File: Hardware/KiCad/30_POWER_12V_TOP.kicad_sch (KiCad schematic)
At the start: 0 parts

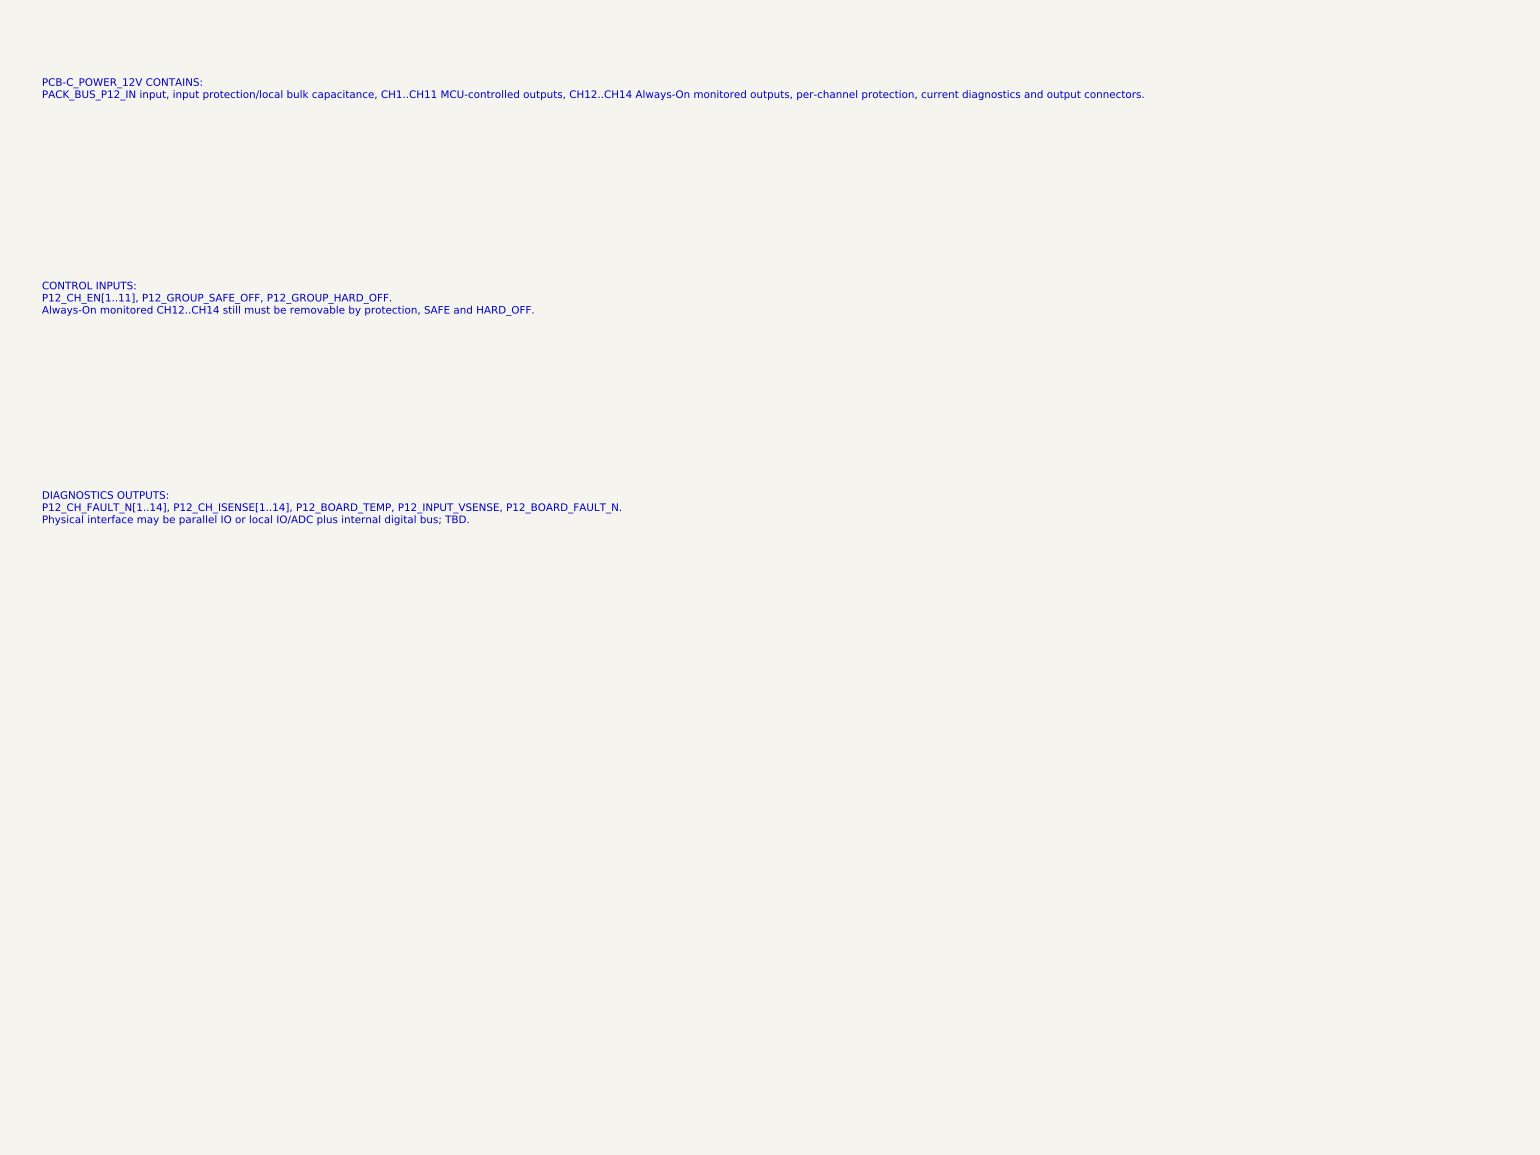
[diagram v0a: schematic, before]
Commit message: hardware: detail all PCB top sheets level A
Convert remaining PCB top sheets to Architecture Level A functional sheets.

Includes PCB-A/BFE_POWER, PCB-B/CTRL_RESERVE, PCB-C/POWER_12V, PCB-D/POWER_5V, PCB-E/LIGHT_POWER, and manifest update.

No component selection, footprints, connector family selection, final pin-count, or PCB layout changes.
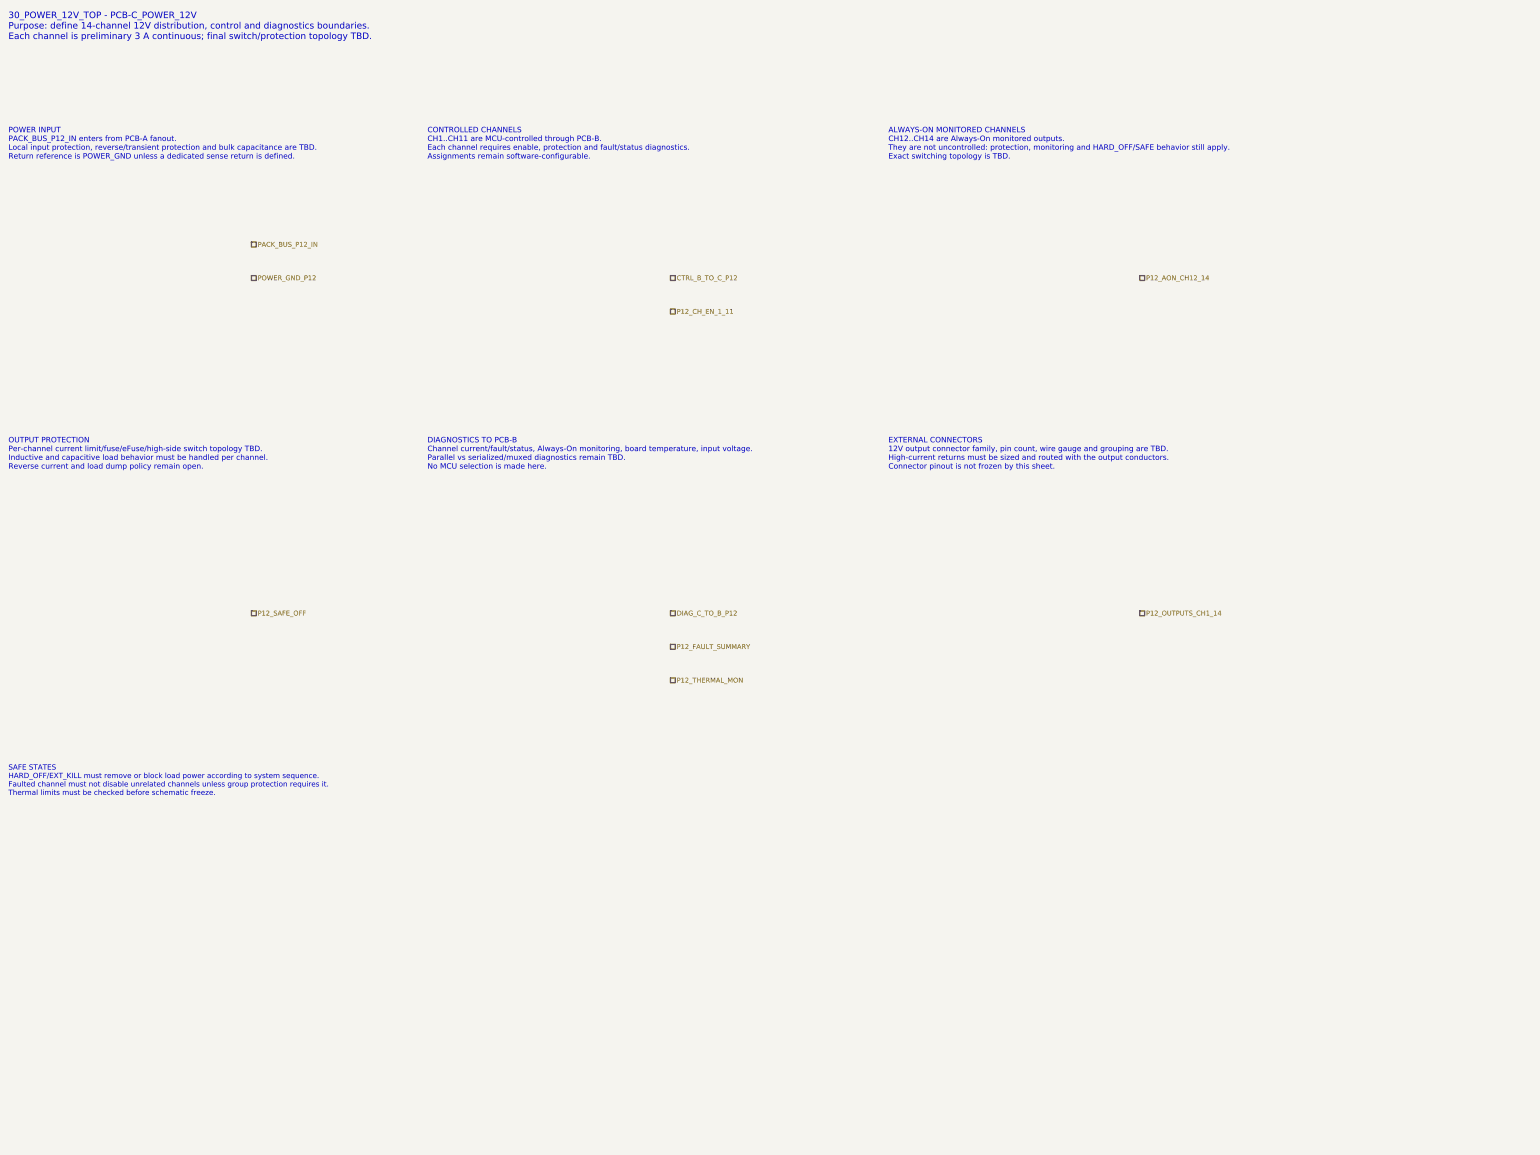
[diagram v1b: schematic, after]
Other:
- note added: "30_POWER_12V_TOP - PCB-C_POWER_12V Purpose: define 14-channel 12V distribution, control and diagnostics boundaries. Each channel is preliminary 3 A continuous; final switch/protection topology TBD."
- note added: "ALWAYS-ON MONITORED CHANNELS CH12..CH14 are Always-On monitored outputs. They are not uncontrolled: protection, monitoring and HARD_OFF/SAFE behavior still apply. Exact switching topology is TBD."
- note added: "CONTROLLED CHANNELS CH1..CH11 are MCU-controlled through PCB-B. Each channel requires enable, protection and fault/status diagnostics. Assignments remain software-configurable."
- note added: "DIAGNOSTICS TO PCB-B Channel current/fault/status, Always-On monitoring, board temperature, input voltage. Parallel vs serialized/muxed diagnostics remain TBD. No MCU selection is made here."
- note added: "EXTERNAL CONNECTORS 12V output connector family, pin count, wire gauge and grouping are TBD. High-current returns must be sized and routed with the output conductors. Connector pinout is not frozen by this sheet."
- note added: "OUTPUT PROTECTION Per-channel current limit/fuse/eFuse/high-side switch topology TBD. Inductive and capacitive load behavior must be handled per channel. Reverse current and load dump policy remain open."
- note added: "POWER INPUT PACK_BUS_P12_IN enters from PCB-A fanout. Local input protection, reverse/transient protection and bulk capacitance are TBD. Return reference is POWER_GND unless a dedicated sense return is defined."
- note added: "SAFE STATES HARD_OFF/EXT_KILL must remove or block load power according to system sequence. Faulted channel must not disable unrelated channels unless group protection requires it. Thermal limits must be checked before schematic freeze."
- note removed: "CONTROL INPUTS: P12_CH_EN[1..11], P12_GROUP_SAFE_OFF, P12_GROUP_HARD_OFF. Always-On monitored CH12..CH14 still must be removable by protection, SAFE and HARD_OFF."
- note removed: "DIAGNOSTICS OUTPUTS: P12_CH_FAULT_N[1..14], P12_CH_ISENSE[1..14], P12_BOARD_TEMP, P12_INPUT_VSENSE, P12_BOARD_FAULT_N. Physical interface may be parallel IO or local IO/ADC plus internal digital bus; TBD."
- note removed: "PCB-C_POWER_12V CONTAINS: PACK_BUS_P12_IN input, input protection/local bulk capacitance, CH1..CH11 MCU-controlled outputs, CH12..CH14 Always-On monitored outputs, per-channel protection, current diagnostics and output connectors."
- company: (none) -> Gonoboben/plataVM
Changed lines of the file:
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@@
 	(title_block
 		(title "30_POWER_12V_TOP - PCB-C_POWER_12V")
-		(date "2026-07-14")
-		(rev "A0")
-		(comment 1 "14-channel 12V distribution, control and diagnostics")
+		(date "2026-07-15")
+		(rev "A1")
+		(company "Gonoboben/plataVM")
+		(comment 1 "Architecture Level A: 14-channel 12V distribution")
+		(comment 2 "No eFuse/high-side switch part numbers or footprints selected")
 	)
-	(text "CONTROL INPUTS:\nP12_CH_EN[1..11], P12_GROUP_SAFE_OFF, P12_GROUP_HARD_OFF.\nAlways-On monitored CH12..CH14 still must be removable by protection, SAFE and HARD_OFF."
+	(text "30_POWER_12V_TOP - PCB-C_POWER_12V\nPurpose: define 14-channel 12V distribution, control and diagnostics boundaries.\nEach channel is preliminary 3 A continuous; final switch/protection topology TBD."
 		(exclude_from_sim no)
-		(at 20 75 0)
-		(effects
-			(font
-				(size 1.8 1.8)
-			)
-			(justify left)
-		)
+		(at 12 10 0)
+		(effects (font (size 1.55 1.55)) (justify left))
+		(uuid "p12-text-0001")
 	)
-	(text "DIAGNOSTICS OUTPUTS:\nP12_CH_FAULT_N[1..14], P12_CH_ISENSE[1..14], P12_BOARD_TEMP, P12_INPUT_VSENSE, P12_BOARD_FAULT_N.\nPhysical interface may be parallel IO or local IO/ADC plus internal digital bus; TBD."
+	(text "POWER INPUT\nPACK_BUS_P12_IN enters from PCB-A fanout.\nLocal input protection, reverse/transient protection and bulk capacitance are TBD.\nReturn reference is POWER_GND unless a dedicated sense return is defined."
 		(exclude_from_sim no)
-		(at 20 125 0)
-		(effects
-			(font
-				(size 1.8 1.8)
-			)
-			(justify left)
-		)
+		(at 12 38 0)
+		(effects (font (size 1.3 1.3)) (justify left))
+		(uuid "p12-text-0002")
 	)
-	(text "PCB-C_POWER_12V CONTAINS:\nPACK_BUS_P12_IN input, input protection/local bulk capacitance, CH1..CH11 MCU-controlled outputs, CH12..CH14 Always-On monitored outputs, per-channel protection, current diagnostics and output connectors."
+	(text "CONTROLLED CHANNELS\nCH1..CH11 are MCU-controlled through PCB-B.\nEach channel requires enable, protection and fault/status diagnostics.\nAssignments remain software-configurable."
 		(exclude_from_sim no)
-		(at 20 25 0)
-		(effects
-			(font
-				(size 1.8 1.8)
-			)
-			(justify left)
-		)
+		(at 112 38 0)
+		(effects (font (size 1.3 1.3)) (justify left))
+		(uuid "p12-text-0003")
 	)
+	(text "ALWAYS-ON MONITORED CHANNELS\nCH12..CH14 are Always-On monitored outputs.\nThey are not uncontrolled: protection, monitoring and HARD_OFF/SAFE behavior still apply.\nExact switching topology is TBD."
+		(exclude_from_sim no)
+		(at 222 38 0)
+		(effects (font (size 1.3 1.3)) (justify left))
+		(uuid "p12-text-0004")
+	)
+	(text "OUTPUT PROTECTION\nPer-channel current limit/fuse/eFuse/high-side switch topology TBD.\nInductive and capacitive load behavior must be handled per channel.\nReverse current and load dump policy remain open."
+		(exclude_from_sim no)
+		(at 12 112 0)
+		(effects (font (size 1.3 1.3)) (justify left))
+		(uuid "p12-text-0005")
+	)
+	(text "DIAGNOSTICS TO PCB-B\nChannel current/fault/status, Always-On monitoring, board temperature, input voltage.\nParallel vs serialized/muxed diagnostics remain TBD.\nNo MCU selection is made here."
+		(exclude_from_sim no)
+		(at 112 112 0)
+		(effects (font (size 1.3 1.3)) (justify left))
+		(uuid "p12-text-0006")
+	)
+	(text "EXTERNAL CONNECTORS\n12V output connector family, pin count, wire gauge and grouping are TBD.\nHigh-current returns must be sized and routed with the output conductors.\nConnector pinout is not frozen by this sheet."
+		(exclude_from_sim no)
+		(at 222 112 0)
+		(effects (font (size 1.3 1.3)) (justify left))
+		(uuid "p12-text-0007")
+	)
+	(text "SAFE STATES\nHARD_OFF/EXT_KILL must remove or block load power according to system sequence.\nFaulted channel must not disable unrelated channels unless group protection requires it.\nThermal limits must be checked before schematic freeze."
+		(exclude_from_sim no)
+		(at 12 190 0)
+		(effects (font (size 1.25 1.25)) (justify left))
+		(uuid "p12-text-0008")
+	)
+	(hierarchical_label "PACK_BUS_P12_IN" (shape passive) (exclude_from_sim no) (at 70 62 0) (effects (font (size 1.15 1.15)) (justify left)) (uuid "p12-label-0001"))
+	(hierarchical_label "POWER_GND_P12" (shape passive) (exclude_from_sim no) (at 70 70 0) (effects (font (size 1.15 1.15)) (justify left)) (uuid "p12-label-0002"))
+	(hierarchical_label "CTRL_B_TO_C_P12" (shape passive) (exclude_from_sim no) (at 170 70 0) (effects (font (size 1.15 1.15)) (justify left)) (uuid "p12-label-0003"))
+	(hierarchical_label "P12_CH_EN_1_11" (shape passive) (exclude_from_sim no) (at 170 78 0) (effects (font (size 1.15 1.15)) (justify left)) (uuid "p12-label-0004"))
+	(hierarchical_label "P12_AON_CH12_14" (shape passive) (exclude_from_sim no) (at 282 70 0) (effects (font (size 1.15 1.15)) (justify left)) (uuid "p12-label-0005"))
+	(hierarchical_label "P12_OUTPUTS_CH1_14" (shape passive) (exclude_from_sim no) (at 282 150 0) (effects (font (size 1.15 1.15)) (justify left)) (uuid "p12-label-0006"))
+	(hierarchical_label "DIAG_C_TO_B_P12" (shape passive) (exclude_from_sim no) (at 170 150 0) (effects (font (size 1.15 1.15)) (justify left)) (uuid "p12-label-0007"))
+	(hierarchical_label "P12_FAULT_SUMMARY" (shape passive) (exclude_from_sim no) (at 170 158 0) (effects (font (size 1.15 1.15)) (justify left)) (uuid "p12-label-0008"))
+	(hierarchical_label "P12_SAFE_OFF" (shape passive) (exclude_from_sim no) (at 70 150 0) (effects (font (size 1.15 1.15)) (justify left)) (uuid "p12-label-0009"))
+	(hierarchical_label "P12_THERMAL_MON" (shape passive) (exclude_from_sim no) (at 170 166 0) (effects (font (size 1.15 1.15)) (justify left)) (uuid "p12-label-0010"))
 )

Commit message: hardware: add PCB-C POWER_12V detailed hierarchy
Merge PCB-C Architecture Level A/B hierarchy after preserving power, control, safe-state, diagnostic, and output boundaries.
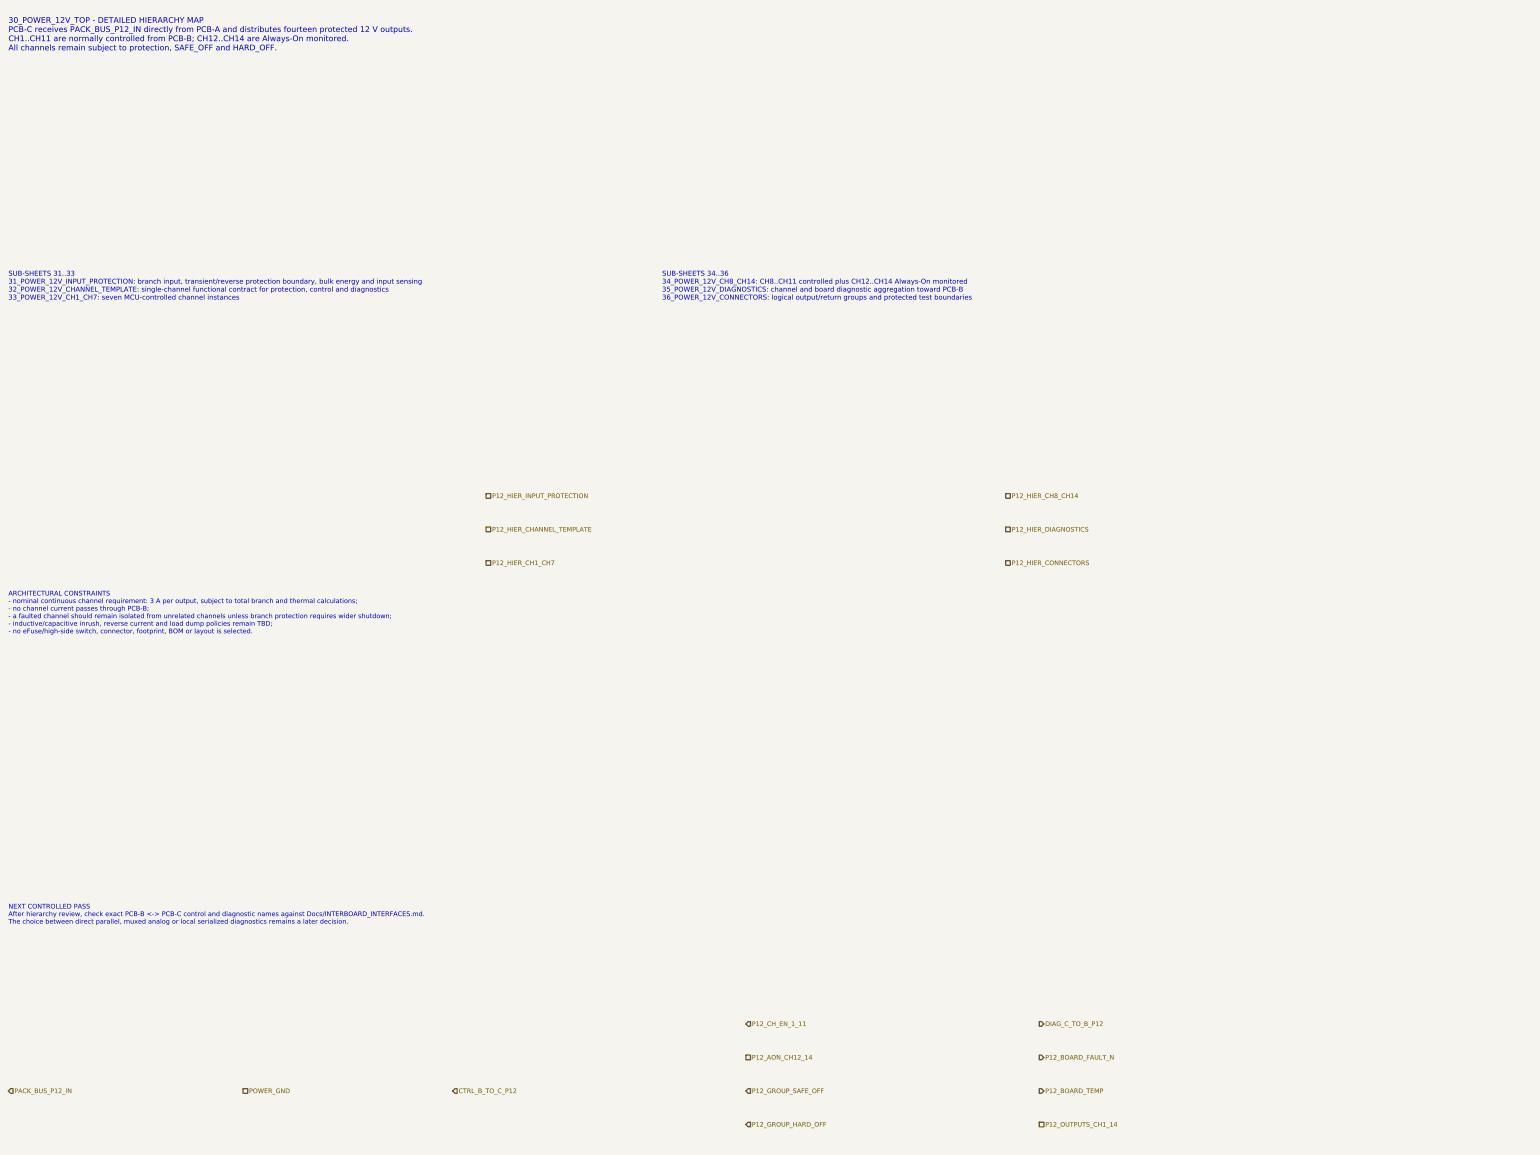
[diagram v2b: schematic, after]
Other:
- note added: "30_POWER_12V_TOP - DETAILED HIERARCHY MAP PCB-C receives PACK_BUS_P12_IN directly from PCB-A and distributes fourteen protected 12 V outputs. CH1..CH11 are normally controlled from PCB-B; CH12..CH14 are Always-On monitored. All channels remain subject to protection, SAFE_OFF and HARD_OFF."
- note added: "ARCHITECTURAL CONSTRAINTS - nominal continuous channel requirement: 3 A per output, subject to total branch and thermal calculations; - no channel current passes through PCB-B; - a faulted channel should remain isolated from unrelated channels unless branch protection requires wider shutdown; - inductive/capacitive inrush, reverse current and load dump policies remain TBD; - no eFuse/high-side sw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"
- note added: "NEXT CONTROLLED PASS After hierarchy review, check exact PCB-B <-> PCB-C control and diagnostic names against Docs/INTERBOARD_INTERFACES.md. The choice between direct parallel, muxed analog or local serialized diagnostics remains a later decision."
- note added: "SUB-SHEETS 31..33 31_POWER_12V_INPUT_PROTECTION: branch input, transient/reverse protection boundary, bulk energy and input sensing 32_POWER_12V_CHANNEL_TEMPLATE: single-channel functional contract for protection, control and diagnostics 33_POWER_12V_CH1_CH7: seven MCU-controlled channel instances"
- note added: "SUB-SHEETS 34..36 34_POWER_12V_CH8_CH14: CH8..CH11 controlled plus CH12..CH14 Always-On monitored 35_POWER_12V_DIAGNOSTICS: channel and board diagnostic aggregation toward PCB-B 36_POWER_12V_CONNECTORS: logical output/return groups and protected test boundaries"
- note removed: "30_POWER_12V_TOP - PCB-C_POWER_12V Purpose: define 14-channel 12V distribution, control and diagnostics boundaries. Each channel is preliminary 3 A continuous; final switch/protection topology TBD."
- note removed: "ALWAYS-ON MONITORED CHANNELS CH12..CH14 are Always-On monitored outputs. They are not uncontrolled: protection, monitoring and HARD_OFF/SAFE behavior still apply. Exact switching topology is TBD."
- note removed: "CONTROLLED CHANNELS CH1..CH11 are MCU-controlled through PCB-B. Each channel requires enable, protection and fault/status diagnostics. Assignments remain software-configurable."
- note removed: "DIAGNOSTICS TO PCB-B Channel current/fault/status, Always-On monitoring, board temperature, input voltage. Parallel vs serialized/muxed diagnostics remain TBD. No MCU selection is made here."
- note removed: "EXTERNAL CONNECTORS 12V output connector family, pin count, wire gauge and grouping are TBD. High-current returns must be sized and routed with the output conductors. Connector pinout is not frozen by this sheet."
- note removed: "OUTPUT PROTECTION Per-channel current limit/fuse/eFuse/high-side switch topology TBD. Inductive and capacitive load behavior must be handled per channel. Reverse current and load dump policy remain open."
- note removed: "POWER INPUT PACK_BUS_P12_IN enters from PCB-A fanout. Local input protection, reverse/transient protection and bulk capacitance are TBD. Return reference is POWER_GND unless a dedicated sense return is defined."
- note removed: "SAFE STATES HARD_OFF/EXT_KILL must remove or block load power according to system sequence. Faulted channel must not disable unrelated channels unless group protection requires it. Thermal limits must be checked before schematic freeze."
